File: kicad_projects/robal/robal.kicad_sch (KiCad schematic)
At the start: 52 parts, among them J1 Conn_01x08, J2 Conn_01x08, J3 Conn_02x08_Odd_Even, J4 Conn_02x05_Odd_Even, J5 Conn_02x02_Odd_Even, J6 Conn_02x02_Odd_Even, J7 Conn_02x02_Odd_Even, J8 Conn_02x02_Odd_Even, U1 NE5532DR, U2 NE5532DR

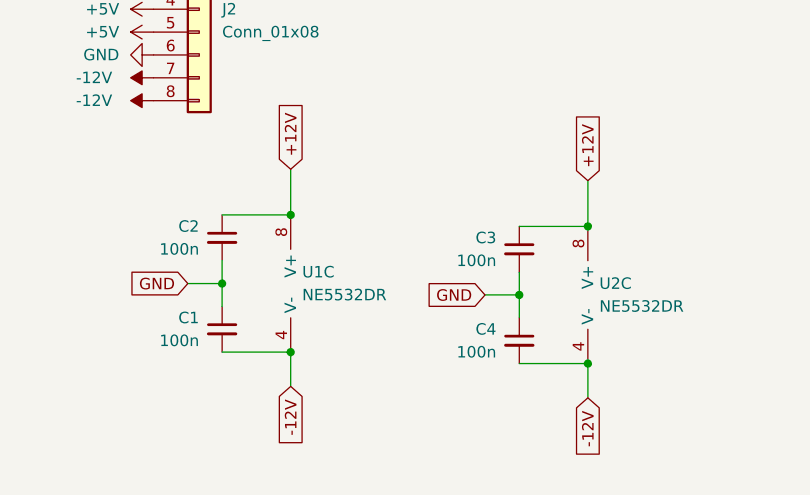
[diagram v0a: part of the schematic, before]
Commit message: Better decoupling caps, red line marker, removed part designators
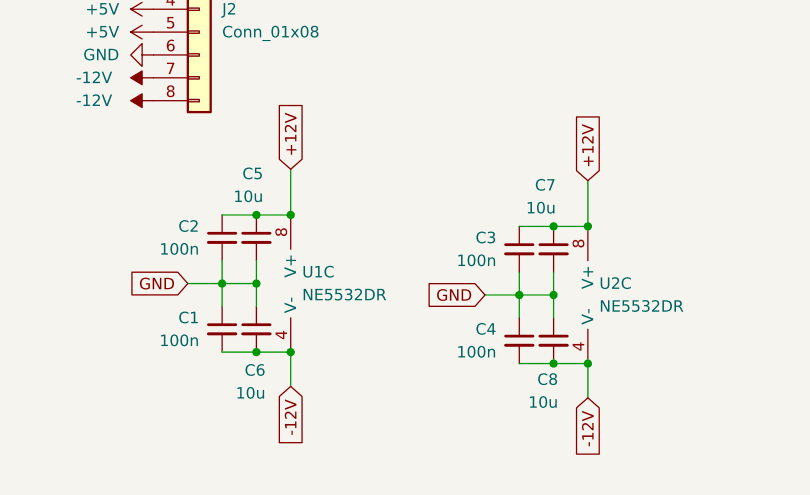
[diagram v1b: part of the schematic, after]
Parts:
- added C5, C6, C7, C8: 10u, Capacitor_SMD:C_0805_2012Metric, symbol Device:C_Small
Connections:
- net +12V: now also C5.1, C7.1
- net -12V: now also C6.2, C8.2
- net GND: now also C5.2, C6.1, C7.2, C8.1
